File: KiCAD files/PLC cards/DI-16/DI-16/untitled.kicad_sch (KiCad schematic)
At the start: 28 parts

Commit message: pcbs
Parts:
- removed D? (x8): LED_Small, symbol Device:LED_Small
- removed J? (x2): Conn_02x06_Odd_Even, symbol Connector_Generic:Conn_02x06_Odd_Even
- removed R? (x8): R_Small, symbol Device:R_Small
- removed RN? (x2): R_Network04, Resistor_THT:R_Array_SIP5, symbol Device:R_Network04
- removed U? (x8): 4N25, Package_DIP:DIP-6_W7.62mm, symbol Isolator:4N25
- added D1, D2, D3, D4, D5, D6, D7, D8: LED_Small, symbol Device:LED_Small
- added J5, J6: Conn_02x06_Odd_Even, symbol Connector_Generic:Conn_02x06_Odd_Even
- added R2, R3, R4, R5, R6, R7, R8, R9: R_Small, symbol Device:R_Small
- added RN2, RN3: (no value), Resistor_THT:R_Array_SIP5, symbol Device:R_Network04
- added RN4: 330, Resistor_THT:R_Array_SIP5, symbol Device:R_Network04
- added RN5: 100k, Resistor_THT:R_Array_SIP5, symbol Device:R_Network04
- added U10, U11, U12, U13, U6, U7, U8, U9: 4N25, Package_DIP:DIP-6_W7.62mm, symbol Isolator:4N25
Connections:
- net +5V: now also RN2.1 (common), RN4.1 (common)
- net D00: now also D4.1 (K), U9.5
- net D01: now also D3.1 (K), U8.5
- net D02: now also D2.1 (K), U7.5
- net D03: now also D1.1 (K), U6.5
- net D04: now also D8.1 (K), U13.5
- net D05: now also D7.1 (K), U12.5
- net D06: now also D6.1 (K), U11.5
- net D07: now also D5.1 (K), U10.5
- net Earth_Protective: now also J5.10 (Pin_10), J5.3 (Pin_3), J5.4 (Pin_4), J5.9 (Pin_9), J6.10 (Pin_10), J6.3 (Pin_3), J6.4 (Pin_4), J6.9 (Pin_9)
- net GND: now also RN3.1 (common), RN5.1 (common), U10.4, U11.4, U12.4, U13.4, U6.4, U7.4, U8.4, U9.4
- new net: R4.1, U8.1
- new net: J5.5 (Pin_5), U8.2
- new net: RN3.4 (R3), U8.6
- new net: RN5.2 (R1), U10.6
- new net: RN5.3 (R2), U11.6
- new net: RN5.4 (R3), U12.6
- new net: RN5.5 (R4), U13.6
- new net: D7.2 (A), RN4.4 (R3)
- new net: R3.1, U7.1
- new net: J5.7 (Pin_7), U7.2
- new net: RN3.3 (R2), U7.6
- new net: R8.1, U12.1
- new net: J6.5 (Pin_5), U12.2
- new net: D8.2 (A), RN4.5 (R4)
- new net: J6.6 (Pin_6), R8.2
- new net: J6.1 (Pin_1), U13.2
- new net: J6.11 (Pin_11), U10.2
- new net: J6.12 (Pin_12), R6.2
- new net: J6.2 (Pin_2), R9.2
- new net: J6.7 (Pin_7), U11.2
- new net: J6.8 (Pin_8), R7.2
- new net: R5.1, U9.1
- new net: J5.1 (Pin_1), U9.2
- new net: RN3.5 (R4), U9.6
- new net: RN3.2 (R1), U6.6
- new net: R7.1, U11.1
- new net: J5.2 (Pin_2), R5.2
- new net: J5.11 (Pin_11), U6.2
- new net: J5.12 (Pin_12), R2.2
- new net: J5.6 (Pin_6), R4.2
- new net: J5.8 (Pin_8), R3.2
- new net: D5.2 (A), RN4.2 (R1)
- new net: D6.2 (A), RN4.3 (R2)
- new net: R2.1, U6.1
- new net: R9.1, U13.1
- new net: D2.2 (A), RN2.3 (R2)
- new net: D1.2 (A), RN2.2 (R1)
- new net: D4.2 (A), RN2.5 (R4)
- new net: D3.2 (A), RN2.4 (R3)
- new net: R6.1, U10.1
- no-connect marks 8 -> 0

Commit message: pcbs
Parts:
- R2, R3, R4, R5, R6, R7, R8, R9: value R_Small -> (none)
- RN2: value (none) -> 330
- RN3: value (none) -> 100k
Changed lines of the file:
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@@
     (stroke (width 0) (type default) (color 0 0 0 0))
   )
-  (wire (pts (xy 118.11 180.34) (xy 118.11 184.15))
+  (wire (pts (xy 151.13 143.51) (xy 151.13 147.32))
     (stroke (width 0) (type default) (color 0 0 0 0))
   )
@@
     (in_bom yes) (on_board yes) (fields_autoplaced)
     (property "Reference" "R8" (id 0) (at 224.79 90.17 90))
-    (property "Value" "R_Small" (id 1) (at 224.79 92.71 90))
+    (property "Value" "" (id 1) (at 224.79 92.71 90))
     (property "Footprint" "" (id 2) (at 224.79 96.52 0)
       (effects (font (size 1.27 1.27)) hide)
@@
       (effects (font (size 1.27 1.27)) (justify left))
     )
-    (property "Value" "" (id 1) (at 67.31 62.4839 0)
+    (property "Value" "100k" (id 1) (at 67.31 62.4839 0)
       (effects (font (size 1.27 1.27)) (justify left))
     )
@@
     (in_bom yes) (on_board yes) (fields_autoplaced)
     (property "Reference" "R5" (id 0) (at 86.36 72.39 90))
-    (property "Value" "R_Small" (id 1) (at 86.36 74.93 90))
+    (property "Value" "" (id 1) (at 86.36 74.93 90))
     (property "Footprint" "" (id 2) (at 86.36 78.74 0)
       (effects (font (size 1.27 1.27)) hide)
@@
     (pin "1")
   )
-  (symbol (lib_id "power:Earth_Protective") (at 118.11 184.15 0) (unit 1)
-    (in_bom yes) (on_board yes) (fields_autoplaced)
-    (property "Reference" "#PWR030" (id 0) (at 124.46 190.5 0)
-      (effects (font (size 1.27 1.27)) hide)
-    )
-    (property "Value" "Earth_Protective" (id 1) (at 129.54 187.96 0)
-      (effects (font (size 1.27 1.27)) hide)
-    )
-    (property "Footprint" "" (id 2) (at 118.11 186.69 0)
-      (effects (font (size 1.27 1.27)) hide)
-    )
-    (property "Datasheet" "~" (id 3) (at 118.11 186.69 0)
+  (symbol (lib_id "power:Earth_Protective") (at 151.13 147.32 0) (unit 1)
+    (in_bom yes) (on_board yes) (fields_autoplaced)
+    (property "Reference" "#PWR030" (id 0) (at 157.48 153.67 0)
+      (effects (font (size 1.27 1.27)) hide)
+    )
+    (property "Value" "Earth_Protective" (id 1) (at 162.56 151.13 0)
+      (effects (font (size 1.27 1.27)) hide)
+    )
+    (property "Footprint" "" (id 2) (at 151.13 149.86 0)
+      (effects (font (size 1.27 1.27)) hide)
+    )
+    (property "Datasheet" "~" (id 3) (at 151.13 149.86 0)
       (effects (font (size 1.27 1.27)) hide)
     )
@@
     (in_bom yes) (on_board yes) (fields_autoplaced)
     (property "Reference" "R2" (id 0) (at 78.74 128.27 90))
-    (property "Value" "R_Small" (id 1) (at 78.74 130.81 90))
+    (property "Value" "" (id 1) (at 78.74 130.81 90))
     (property "Footprint" "" (id 2) (at 78.74 134.62 0)
       (effects (font (size 1.27 1.27)) hide)
@@
     (pin "1")
   )
-  (symbol (lib_id "power:PWR_FLAG") (at 118.11 180.34 0) (unit 1)
-    (in_bom yes) (on_board yes) (fields_autoplaced)
-    (property "Reference" "#FLG03" (id 0) (at 118.11 178.435 0)
-      (effects (font (size 1.27 1.27)) hide)
-    )
-    (property "Value" "" (id 1) (at 118.11 175.26 0))
-    (property "Footprint" "" (id 2) (at 118.11 180.34 0)
-      (effects (font (size 1.27 1.27)) hide)
-    )
-    (property "Datasheet" "~" (id 3) (at 118.11 180.34 0)
+  (symbol (lib_id "power:PWR_FLAG") (at 151.13 143.51 0) (unit 1)
+    (in_bom yes) (on_board yes) (fields_autoplaced)
+    (property "Reference" "#FLG03" (id 0) (at 151.13 141.605 0)
+      (effects (font (size 1.27 1.27)) hide)
+    )
+    (property "Value" "PWR_FLAG" (id 1) (at 151.13 138.43 0))
+    (property "Footprint" "" (id 2) (at 151.13 143.51 0)
+      (effects (font (size 1.27 1.27)) hide)
+    )
+    (property "Datasheet" "~" (id 3) (at 151.13 143.51 0)
       (effects (font (size 1.27 1.27)) hide)
     )
@@
     (in_bom yes) (on_board yes) (fields_autoplaced)
     (property "Reference" "R9" (id 0) (at 227.33 71.12 90))
-    (property "Value" "R_Small" (id 1) (at 227.33 73.66 90))
+    (property "Value" "" (id 1) (at 227.33 73.66 90))
     (property "Footprint" "" (id 2) (at 227.33 77.47 0)
       (effects (font (size 1.27 1.27)) hide)
@@
     (in_bom yes) (on_board yes) (fields_autoplaced)
     (property "Reference" "R4" (id 0) (at 83.82 91.44 90))
-    (property "Value" "R_Small" (id 1) (at 83.82 93.98 90))
+    (property "Value" "" (id 1) (at 83.82 93.98 90))
     (property "Footprint" "" (id 2) (at 83.82 97.79 0)
       (effects (font (size 1.27 1.27)) hide)
@@
     (in_bom yes) (on_board yes) (fields_autoplaced)
     (property "Reference" "R3" (id 0) (at 81.28 110.49 90))
-    (property "Value" "R_Small" (id 1) (at 81.28 113.03 90))
+    (property "Value" "" (id 1) (at 81.28 113.03 90))
     (property "Footprint" "" (id 2) (at 81.28 116.84 0)
       (effects (font (size 1.27 1.27)) hide)
@@
       (effects (font (size 1.27 1.27)) (justify left))
     )
-    (property "Value" "" (id 1) (at 48.26 62.4839 0)
+    (property "Value" "330" (id 1) (at 48.26 62.4839 0)
       (effects (font (size 1.27 1.27)) (justify left))
     )
@@
     (in_bom yes) (on_board yes) (fields_autoplaced)
     (property "Reference" "R6" (id 0) (at 219.71 127 90))
-    (property "Value" "R_Small" (id 1) (at 219.71 129.54 90))
+    (property "Value" "" (id 1) (at 219.71 129.54 90))
     (property "Footprint" "" (id 2) (at 219.71 133.35 0)
       (effects (font (size 1.27 1.27)) hide)
@@
     (in_bom yes) (on_board yes) (fields_autoplaced)
     (property "Reference" "R7" (id 0) (at 222.25 109.22 90))
-    (property "Value" "R_Small" (id 1) (at 222.25 111.76 90))
+    (property "Value" "" (id 1) (at 222.25 111.76 90))
     (property "Footprint" "" (id 2) (at 222.25 115.57 0)
       (effects (font (size 1.27 1.27)) hide)

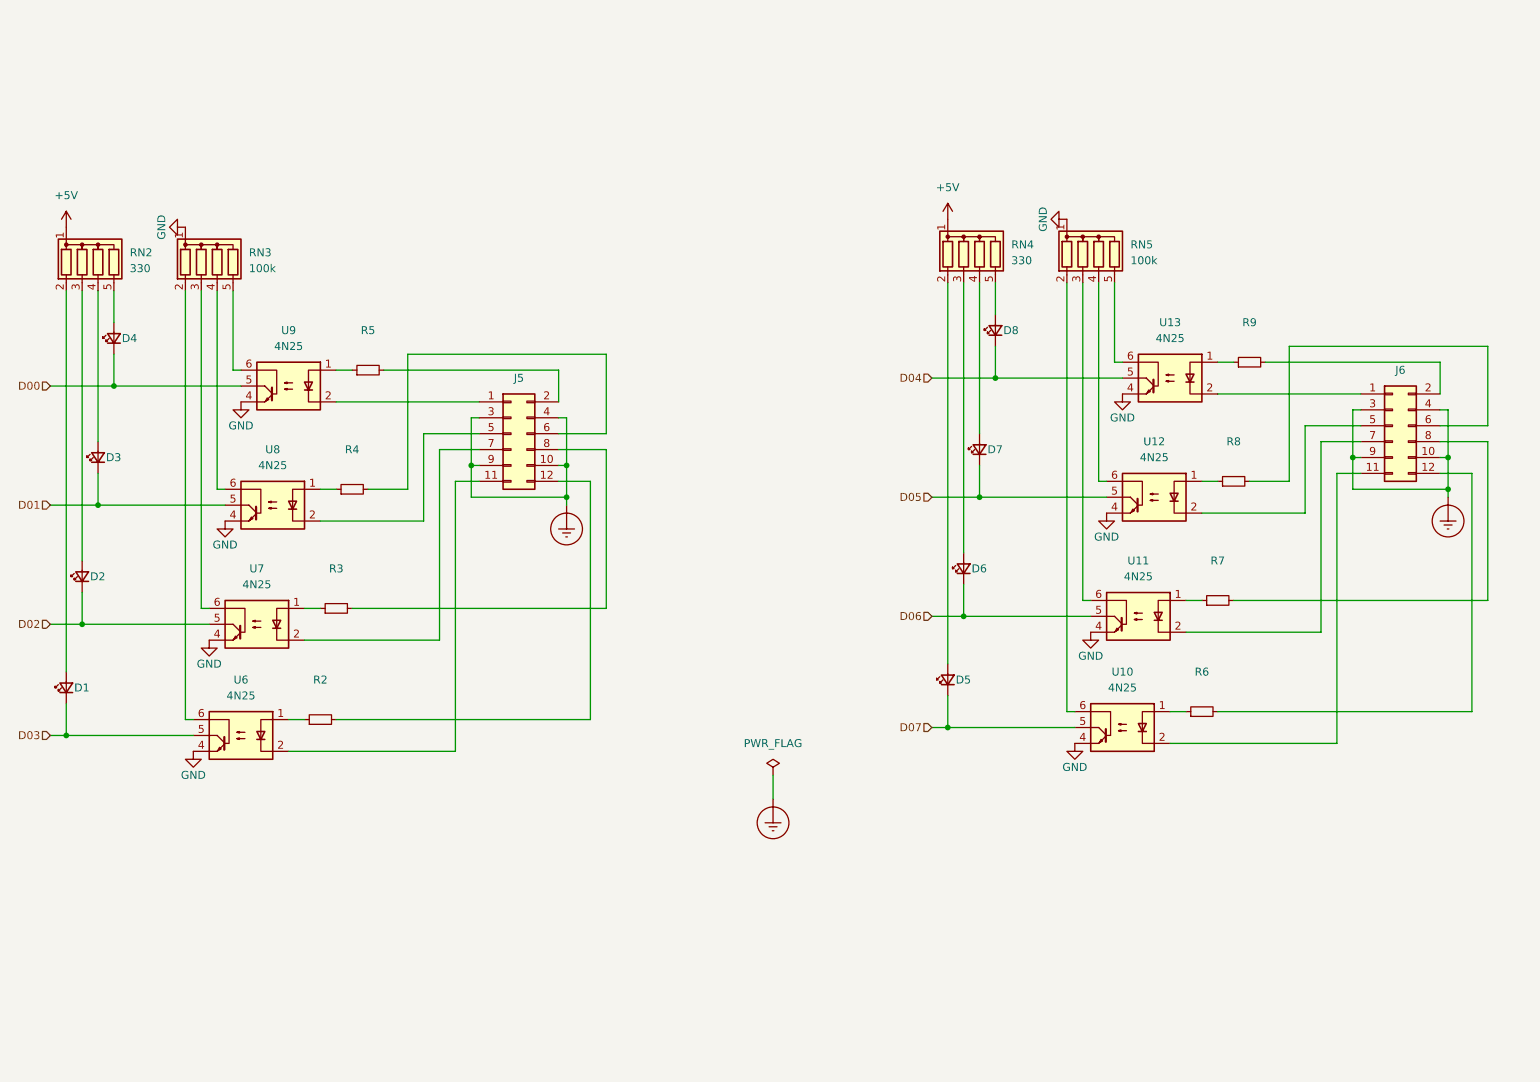
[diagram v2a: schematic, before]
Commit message: DI & DO updates
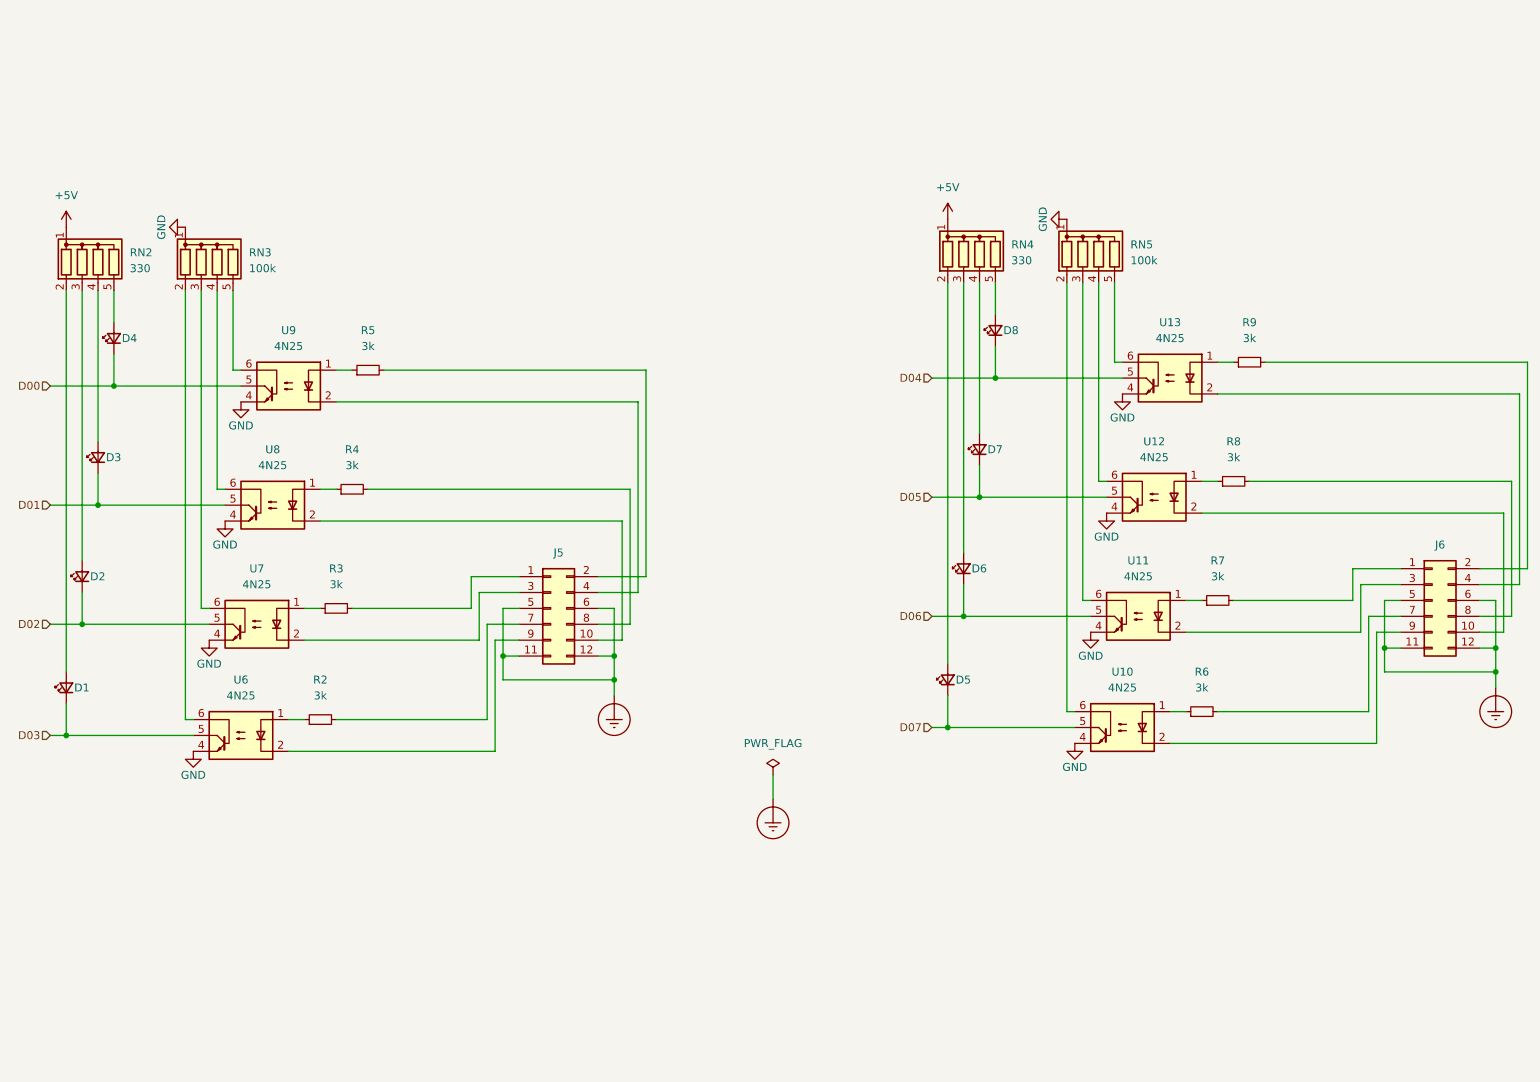
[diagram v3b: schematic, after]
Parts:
- R2, R3, R4, R5, R6, R7, R8, R9: value (none) -> 3k
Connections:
- net Earth_Protective: now also J5.11 (Pin_11), J5.12 (Pin_12), J5.5 (Pin_5), J5.6 (Pin_6), J6.11 (Pin_11), J6.12 (Pin_12), J6.5 (Pin_5), J6.6 (Pin_6); no longer J5.10 (Pin_10), J5.3 (Pin_3), J5.4 (Pin_4), J5.9 (Pin_9), J6.10 (Pin_10), J6.3 (Pin_3), J6.4 (Pin_4), J6.9 (Pin_9)
- net at U8.2: now also J5.10 (Pin_10); no longer J5.5 (Pin_5)
- net at U7.2: now also J5.3 (Pin_3); no longer J5.7 (Pin_7)
- net at U12.2: now also J6.10 (Pin_10); no longer J6.5 (Pin_5)
- net at R8.2: now also J6.8 (Pin_8); no longer J6.6 (Pin_6)
- net at U13.2: now also J6.4 (Pin_4); no longer J6.1 (Pin_1)
- net at U10.2: now also J6.9 (Pin_9); no longer J6.11 (Pin_11)
- net at R6.2: now also J6.7 (Pin_7); no longer J6.12 (Pin_12)
- net at U11.2: now also J6.3 (Pin_3); no longer J6.7 (Pin_7)
- net at R7.2: now also J6.1 (Pin_1); no longer J6.8 (Pin_8)
- net at U9.2: now also J5.4 (Pin_4); no longer J5.1 (Pin_1)
- net at U6.2: now also J5.9 (Pin_9); no longer J5.11 (Pin_11)
- net at R2.2: now also J5.7 (Pin_7); no longer J5.12 (Pin_12)
- net at R4.2: now also J5.8 (Pin_8); no longer J5.6 (Pin_6)
- net at R3.2: now also J5.1 (Pin_1); no longer J5.8 (Pin_8)
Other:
- moved on the sheet: J5
